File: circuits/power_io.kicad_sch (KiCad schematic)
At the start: 39 parts, among them J3 ADC debug, J4 LASER+MPD out, J5 LASER PSU, J6 EXT 5V, U11 AP2112K-3.3, U12 INA4180A1, U13 LM4040C50 5V, U14 AD7606BSTZ-4

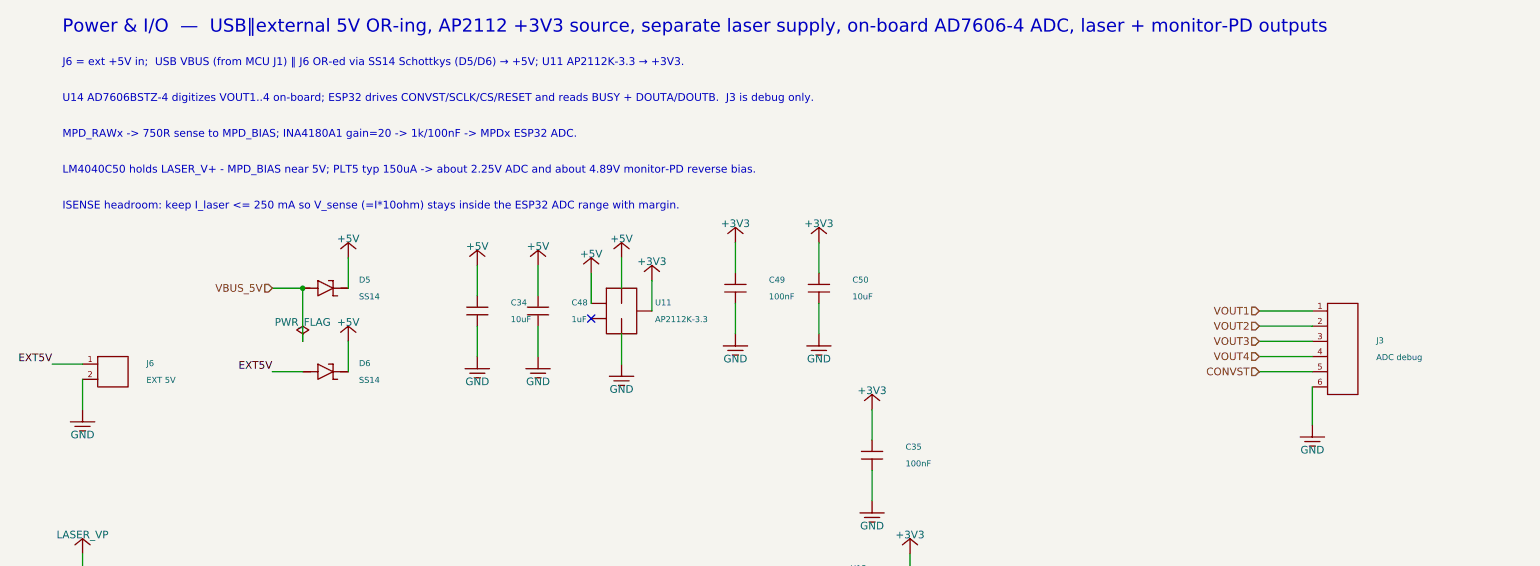
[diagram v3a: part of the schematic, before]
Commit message: fix pcb update footprint identity
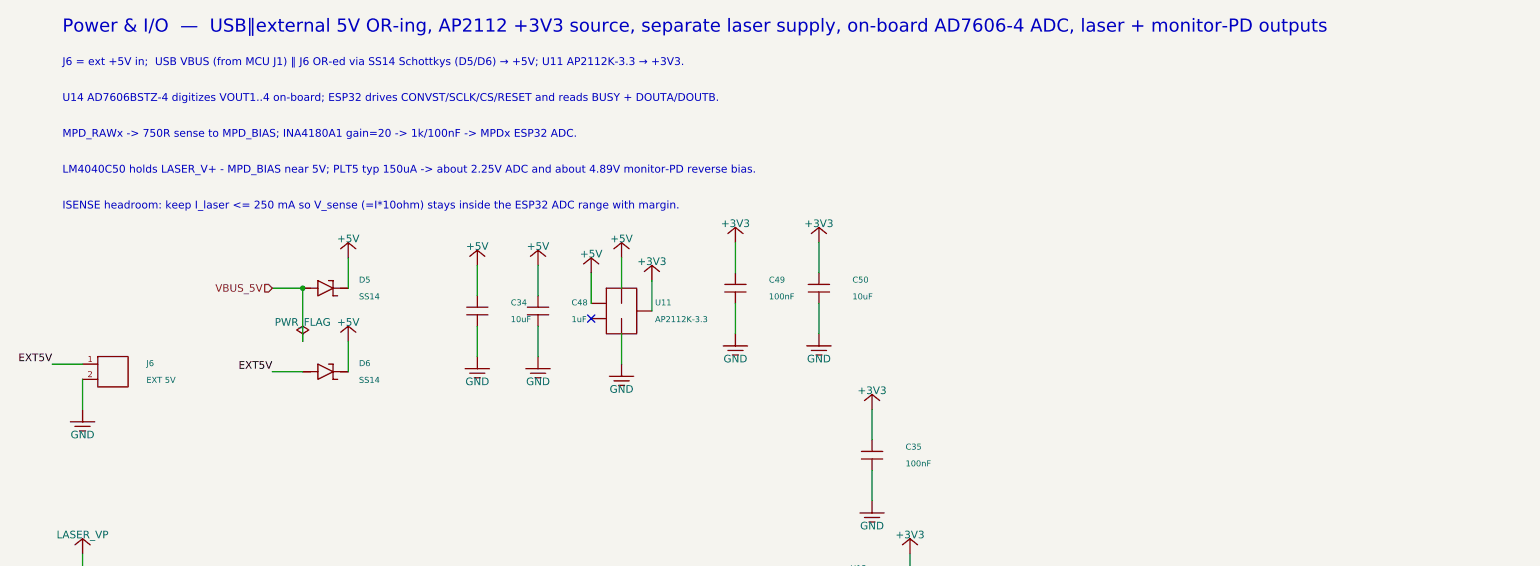
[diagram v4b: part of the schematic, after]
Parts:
- removed C36: 100nF MPD bias, Capacitor_SMD:C_0402_1005Metric_Pad0.74x0.62mm_HandSolder, symbol viv:C_V
- removed U14: AD7606BSTZ-4, Package_QFP:LQFP-64_10x10mm_P0.5mm, symbol viv:AD7606_4
- added U13: LM4040C50 5V, Package_TO_SOT_SMD:SOT-23, symbol viv:LM4040_DBZ
- C36: renamed from U13; value LM4040C50 5V -> 100nF MPD bias; footprint Package_TO_SOT_SMD:SOT-23 -> Capacitor_SMD:C_0402_1005Metric_Pad0.74x0.62mm_HandSolder; symbol viv:LM4040_DBZ -> viv:C_V; LCSC C69316 -> C83056; Part Number LM4040C50IDBZR -> 0402B104K160CT
- U14: renamed from J3; value ADC debug -> AD7606BSTZ-4; footprint Connector_PinHeader_2.54mm:PinHeader_1x06_P2.54mm_Vertical -> Package_QFP:LQFP-64_10x10mm_P0.5mm; symbol viv:CONN6 -> viv:AD7606_4; LCSC (none) -> C51512; Part Number (none) -> AD7606BSTZ-4RL
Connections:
- net +3V3: now also U14.23 (VDRIVE), U14.34 (REF SELECT), U14.6 (PAR/SER/BYTE SEL), U14.7 (STBY)
- net +5V: now also U14.1 (AVCC), U14.37 (AVCC), U14.38 (AVCC), U14.48 (AVCC)
- net ADC_BUSY: now also U14.14 (BUSY)
- net ADC_CS: now also U14.13 (CS)
- net ADC_MISO_A: now also U14.24 (DB7/DOUTA)
- net ADC_MISO_B: now also U14.25 (DB8/DOUTB)
- net ADC_RESET: now also U14.11 (RESET)
- net ADC_SCLK: now also U14.12 (RD/SCLK)
- net CONVST: now also U14.10 (CONVSTB), U14.9 (CONVSTA); no longer U14.5
- net GND: now also U14.16 (DB0), U14.17 (DB1), U14.18 (DB2), U14.19 (DB3), U14.2 (AGND), U14.20 (DB4), U14.21 (DB5), U14.22 (DB6), U14.26 (AGND), U14.27 (DB9), U14.28 (DB10), U14.29 (DB11), U14.3 (OS0), U14.30 (DB12), U14.31 (DB13), U14.32 (DB14/HBEN), U14.33 (DB15/BYTE SEL), U14.35 (AGND), U14.4 (OS1), U14.40 (AGND), U14.41 (AGND), U14.43 (REFGND), U14.46 (REFGND), U14.47 (AGND), U14.5 (OS2), U14.50 (V1GND), U14.52 (V2GND), U14.53 (AGND), U14.54 (AGND), U14.55 (AGND), U14.56 (AGND), U14.58 (V3GND), U14.60 (V4GND), U14.61 (AGND), U14.62 (AGND), U14.63 (AGND), U14.64 (AGND), U14.8 (RANGE), U13.1 (K); no longer U14.6
- net MPD_BIAS: now also U13.2 (A), U13.3 (*); no longer C36.3 (*)
- net VOUT1: now also U14.49 (V1); no longer U14.1
- net VOUT2: now also U14.51 (V2); no longer U14.2
- net VOUT3: now also U14.57 (V3); no longer U14.3
- net VOUT4: now also U14.59 (V4); no longer U14.4
- net at C57.1: now also U14.36 (REGCAP)
- net at C58.1: now also U14.39 (REGCAP)
- net at C59.1: now also U14.42 (REFIN/REFOUT)
- net at C60.1: now also U14.44 (REFCAPA), U14.45 (REFCAPB)
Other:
- note added: "U14 AD7606BSTZ-4 digitizes VOUT1..4 on-board; ESP32 drives CONVST/SCLK/CS/RESET and reads BUSY + DOUTA/DOUTB."
- note removed: "U14 AD7606BSTZ-4 digitizes VOUT1..4 on-board; ESP32 drives CONVST/SCLK/CS/RESET and reads BUSY + DOUTA/DOUTB. J3 is debug only."

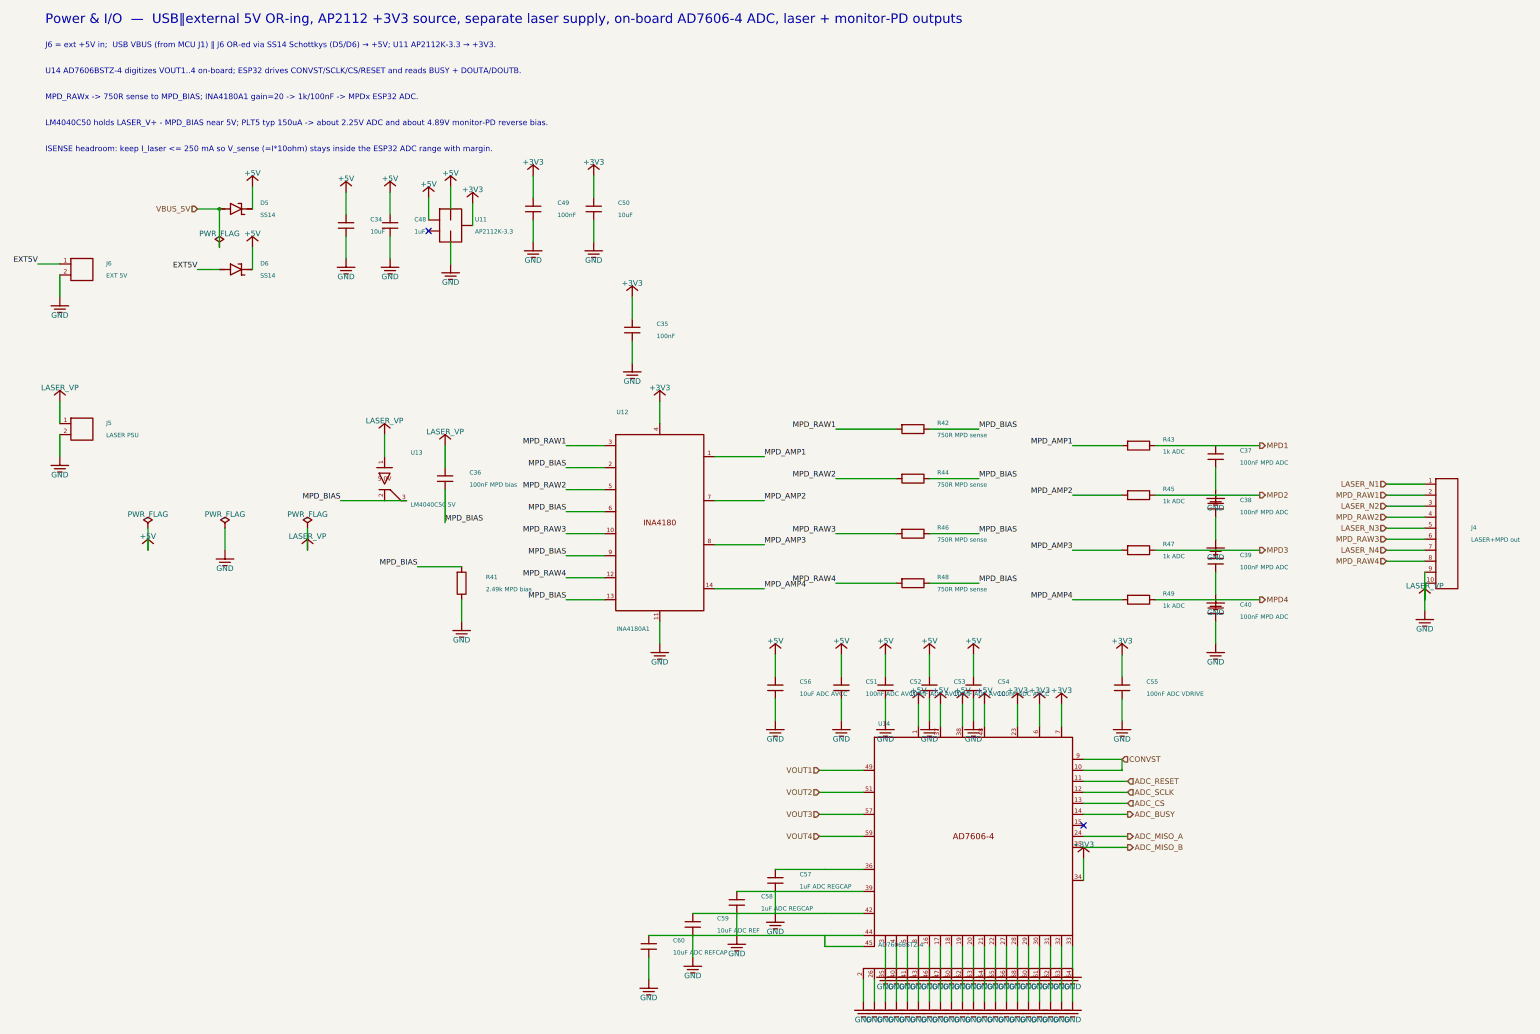
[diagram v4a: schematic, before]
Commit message: save current laser controller recovery state
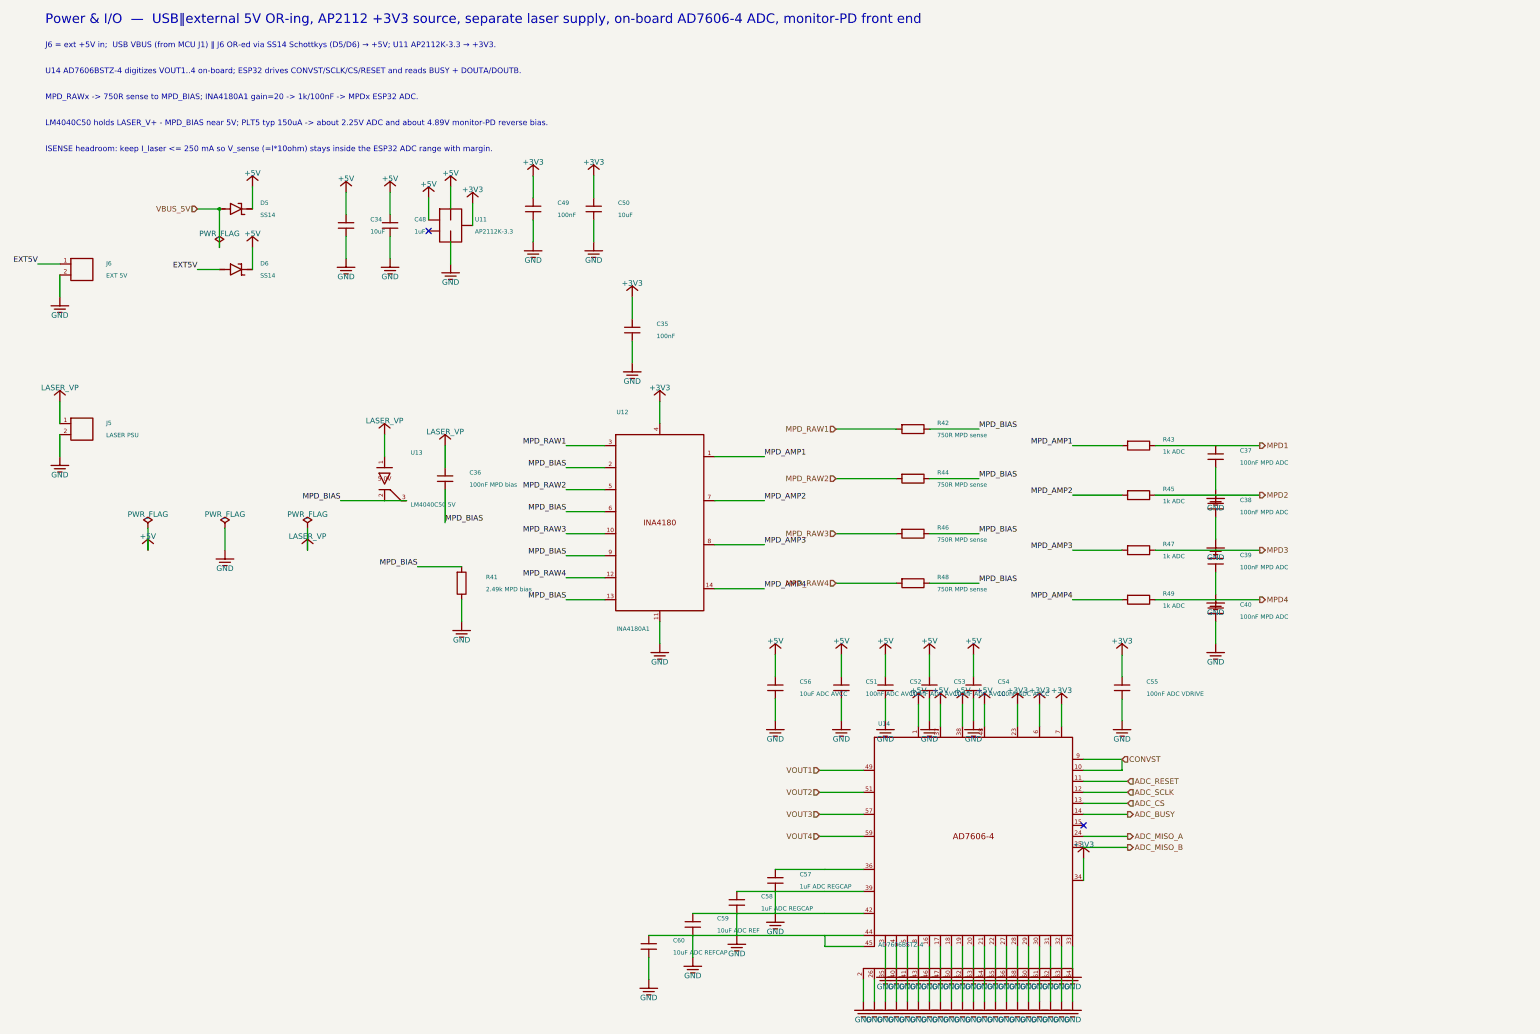
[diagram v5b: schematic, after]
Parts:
- removed U12: INA4180A1, Package_SO:TSSOP-14_4.4x5mm_P0.65mm, symbol viv:INA4180_TSSOP14
- U12: renamed from J4; value LASER+MPD out -> INA4180A1; footprint Connector_PinHeader_2.54mm:PinHeader_1x10_P2.54mm_Vertical -> Package_SO:TSSOP-14_4.4x5mm_P0.65mm; symbol viv:CONN10 -> viv:INA4180_TSSOP14; LCSC (none) -> C2057528; Part Number (none) -> INA4180A1IPWR
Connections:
- net LASER_N1 is gone; now on net MPD_AMP1: U12.1 (OUT1)
- net LASER_N2 is gone; now on net MPD_RAW1: U12.3 (IN+1)
- net LASER_N3 is gone; now on net MPD_RAW2: U12.5 (IN+2)
- net LASER_N4 is gone; now on net MPD_AMP2: U12.7 (OUT2)
- net +3V3: now also U12.4 (VS)
- net GND: now also U12.11 (GND); no longer C36.1, J5.1, U12.10, U12.9, U13.1 (K)
- net MPD_AMP3: now also U12.8 (OUT3)
- net MPD_AMP4: now also U12.14 (OUT4)
- net MPD_BIAS: now also U12.13 (IN-4), U12.2 (IN-1), U12.6 (IN-2), U12.9 (IN-3)
- net MPD_RAW1: no longer U12.2
- net MPD_RAW2: no longer U12.4
- net MPD_RAW3: now also U12.10 (IN+3); no longer U12.6
- net MPD_RAW4: now also U12.12 (IN+4); no longer U12.8
- new net LASER_V+: C36.1, J5.1, U13.1 (K)
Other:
- note added: "Power & I/O — USB‖external 5V OR-ing, AP2112 +3V3 source, separate laser supply, on-board AD7606-4 ADC, monitor-PD front end"
- note removed: "Power & I/O — USB‖external 5V OR-ing, AP2112 +3V3 source, separate laser supply, on-board AD7606-4 ADC, laser + monitor-PD outputs"
